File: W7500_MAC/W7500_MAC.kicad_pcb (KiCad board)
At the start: 2 copper layers, 43 x 37.5 mm, 22 parts, among them IC1 W7500, J1 Conn_02x05_Odd_Even, J2 Conn_02x05_Odd_Even, J3 Conn_02x11_Odd_Even, J4 Conn_02x06_Odd_Even, J5 Conn_02x06_Odd_Even, Y1 8MHz

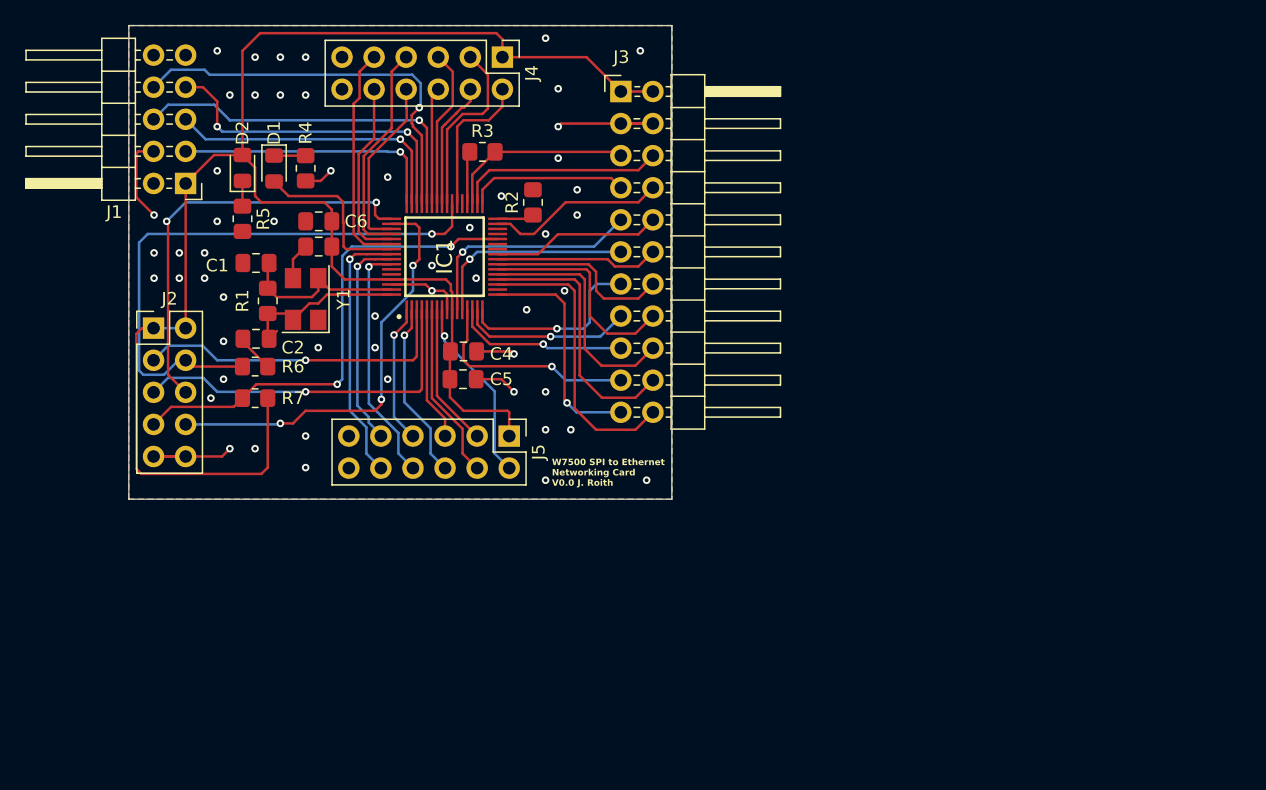
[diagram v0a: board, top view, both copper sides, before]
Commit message: W7500 MAC redesign to manufactured version
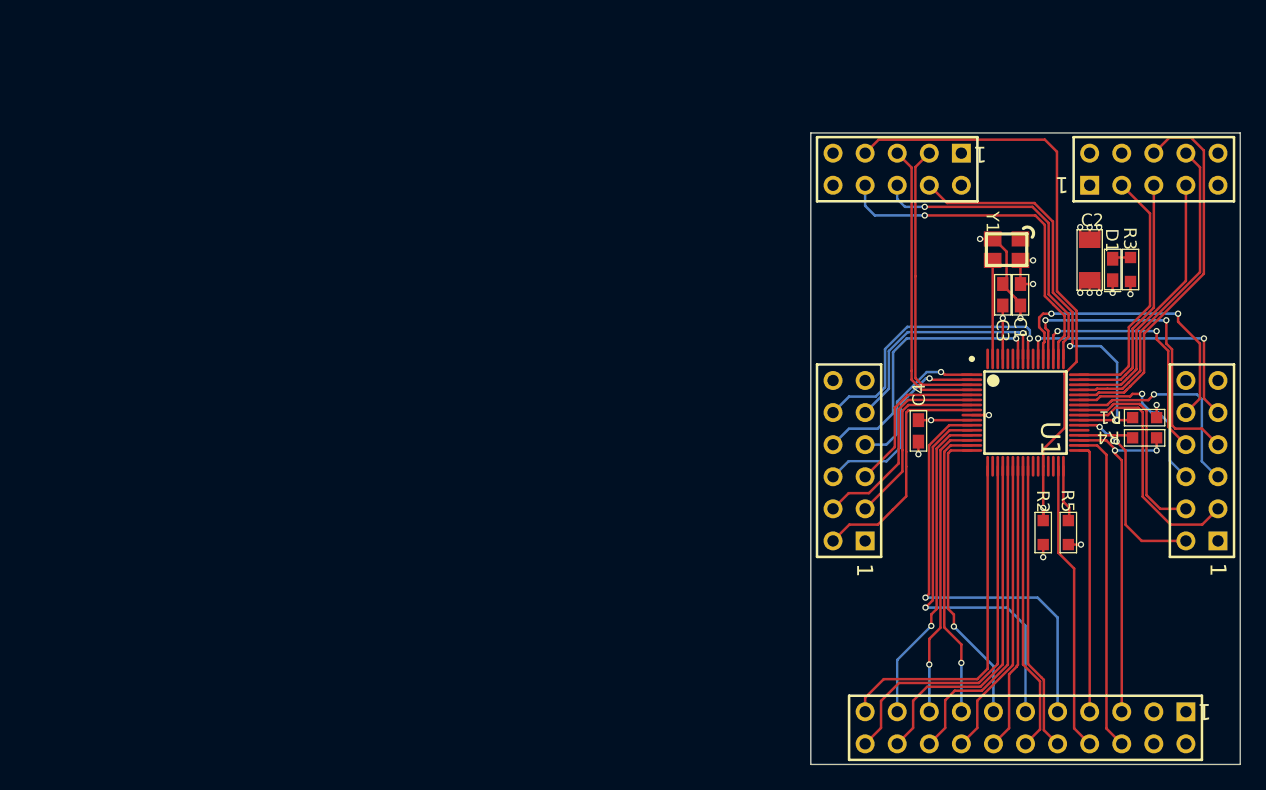
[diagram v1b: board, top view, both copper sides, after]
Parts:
- removed C5: 10u, Capacitor_SMD:C_0805_2012Metric_Pad1.18x1.45mm_HandSolder
- removed C6: 1u, Capacitor_SMD:C_0805_2012Metric_Pad1.18x1.45mm_HandSolder
- removed D2: LED, LED_SMD:LED_0805_2012Metric_Pad1.15x1.40mm_HandSolder
- removed IC1: W7500, SamacSys_Parts:QFP40P900X900X160-64N
- removed J1: Conn_02x05_Odd_Even, Connector_PinHeader_2.54mm:PinHeader_2x05_P2.54mm_Horizontal
- removed J2: Conn_02x05_Odd_Even, Connector_PinHeader_2.54mm:PinHeader_2x05_P2.54mm_Vertical
- removed J3: Conn_02x11_Odd_Even, Connector_PinHeader_2.54mm:PinHeader_2x11_P2.54mm_Horizontal
- removed J4, J5: Conn_02x06_Odd_Even, Connector_PinHeader_2.54mm:PinHeader_2x06_P2.54mm_Vertical
- removed R6, R7: 4.7k, Resistor_SMD:R_0805_2012Metric_Pad1.20x1.40mm_HandSolder
- added P1: Header 5X2, Miscellaneous Connectors:HDR2X5, F.Cu at (143.4, 81.6)
- added P2: Header 6X2, Miscellaneous Connectors:HDR2X6, F.Cu at (163.7, 112.3)
- added P3: Header 6X2, Miscellaneous Connectors:HDR2X6, F.Cu at (135.8, 112.3)
- added P4: Header 5X2, Miscellaneous Connectors:HDR2X5, F.Cu at (153.6, 84.1)
- added P5: Header 11X2H, Miscellaneous Connectors:HDR2X11, F.Cu at (161.2, 125.8)
- added U1: W7500, pcSwitchLib:W7500_64pin, F.Cu at (148.5, 102.1)
- C1: value 18p -> 100nF 0603; footprint Capacitor_SMD:C_0805_2012Metric_Pad1.18x1.45mm_HandSolder -> pcSwitchLib:0603_CAP
- C2: value 18p -> 10uF 1206; footprint Capacitor_SMD:C_0805_2012Metric_Pad1.18x1.45mm_HandSolder -> pcSwitchLib:1206_CAP
- C3: value 10u -> 100nF 0603; footprint Capacitor_SMD:C_0805_2012Metric_Pad1.18x1.45mm_HandSolder -> pcSwitchLib:0603_CAP
- C4: value 1u -> 100nF 0603; footprint Capacitor_SMD:C_0805_2012Metric_Pad1.18x1.45mm_HandSolder -> pcSwitchLib:0603_CAP
- D1: value LED -> LED0; footprint LED_SMD:LED_0805_2012Metric_Pad1.15x1.40mm_HandSolder -> pcSwitchLib:0603_LED
- R1: value 1M -> 4k7 0603; footprint Resistor_SMD:R_0805_2012Metric_Pad1.20x1.40mm_HandSolder -> pcSwitchLib:0603
- R2: value 4.7k -> 4k7 0603; footprint Resistor_SMD:R_0805_2012Metric_Pad1.20x1.40mm_HandSolder -> pcSwitchLib:0603
- R3: value 500 -> 330R 0603; footprint Resistor_SMD:R_0805_2012Metric_Pad1.20x1.40mm_HandSolder -> pcSwitchLib:0603
- R4: value R -> 330R 0603; footprint Resistor_SMD:R_0805_2012Metric_Pad1.20x1.40mm_HandSolder -> pcSwitchLib:0603
- R5: value 500 -> 4k7 0603; footprint Resistor_SMD:R_0805_2012Metric_Pad1.20x1.40mm_HandSolder -> pcSwitchLib:0603
- Y1: value 8MHz -> 8MHz 3225; footprint Crystal:Crystal_SMD_5032-4Pin_5.0x3.2mm -> pcSwitchLib:XTAL_3225
- moved R1 70.0 mm to (157.9, 102.5), turned to 180 degrees
- moved R5 70.0 mm to (151.9, 111.6), turned to 90 degrees
- moved R4 69.8 mm to (157.9, 104.1), turned to 180 degrees
- moved D1 66.9 mm to (155.4, 90.8)
- moved C2 66.3 mm to (153.6, 90.1), turned to 90 degrees
- moved C1 60.6 mm to (148.1, 92.8), turned to 90 degrees
- moved Y1 55.6 mm to (147.0, 89.2), turned to 180 degrees
- moved C3 54.3 mm to (146.7, 92.8), turned to -90 degrees
- moved R3 52.1 mm to (156.8, 90.8), turned to -90 degrees
- moved R2 48.1 mm to (149.9, 111.6), turned to -90 degrees
- moved C4 36.6 mm to (140.0, 103.6), turned to 90 degrees
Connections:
- C1 pad 1: XIN -> GND
- C1 pad 2: GND -> VCC_3V3
- C2 pad 1: XOUT -> GND
- C2 pad 2: GND -> VCC_3V3
- C3 pad 1: +3V3 -> GND
- C3 pad 2: GND -> VCC_3V3
- C4 pad 1: +3V3 -> GND
- C4 pad 2: GND -> VCC_3V3
- D1 pad 1: Net-(D1-K) -> NetD1_1
- D1 pad 2: PC_02 -> GND
- R1 pad 1: XIN -> GND
- R1 pad 2: XOUT -> BOOT
- R2 pad 1: Net-(IC1-TEST) -> RESET
- R2 pad 2: GND -> VCC_3V3
- R3 pad 1: Net-(IC1-PA_08) -> NetD1_1
- R3 pad 2: /MII Connector/MDIO -> VCC_3V3
- R4 pad 1: Net-(D1-K) -> MDIO
- R4 pad 2: GND -> NetR4_2
- R5 pad 1: Net-(D2-K) -> GND
- R5 pad 2: GND -> TEST
- Y1 pad 1: GND -> (no net)
- Y1 pad 2: XIN -> GND
- Y1 pad 3: GND -> NetU1_63
- Y1 pad 4: XOUT -> VCC_3V3
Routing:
- net +3V3: track 132.8 -> 0.00 mm
- net RESET: track 0.00 -> 47.9 mm, vias 0 -> 1
- net /Debug Interfaces/BOOT: track 46.3 -> 0.00 mm, vias 1 -> 0
- net /Debug Interfaces/~{RESET}: track 39.0 -> 0.00 mm, vias 2 -> 0
- net CRS: track 0.00 -> 34.8 mm, vias 0 -> 1
- net BOOT: track 0.00 -> 34.6 mm, vias 0 -> 2
- net /Debug Interfaces/SWD_SWDCLK: track 33.8 -> 0.00 mm, vias 2 -> 0
- net /Debug Interfaces/SWD_SWDIO: track 33.7 -> 0.00 mm, vias 3 -> 0
- net /SPI & IRQ Connector/~{CS}: track 32.3 -> 0.00 mm, vias 1 -> 0
- net RXDV: track 0.00 -> 31.9 mm, vias 0 -> 1
- net IRQ: track 0.00 -> 30.3 mm
- net TXCLK: track 0.00 -> 30.0 mm
- net GND: track 46.5 -> 16.8 mm, vias 54 -> 10
- net /SPI & IRQ Connector/IRQ: track 28.9 -> 0.00 mm, vias 1 -> 0
- net /Debug Interfaces/ISP_RXD: track 28.6 -> 0.00 mm, vias 1 -> 0
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- added copper zone on In1.Cu, net GND
- added copper zone on In2.Cu, net VCC_3V3
- removed copper zone on B.Cu, net GND
- removed copper zone on F.Cu, net GND
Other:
- board size 43 x 37.5 mm -> 34 x 50 mm
- copper layers 2 -> 4
- rule pad_to_mask_clearance: 0 -> 0.075
- board text removed: "W7500 SPI to Ethernet Networking Card V0.0 J. Roith"
